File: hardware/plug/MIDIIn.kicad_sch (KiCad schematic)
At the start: 7 parts, among them J401 SJ2-25404B-SMT-TR, U401 74AHC1G125

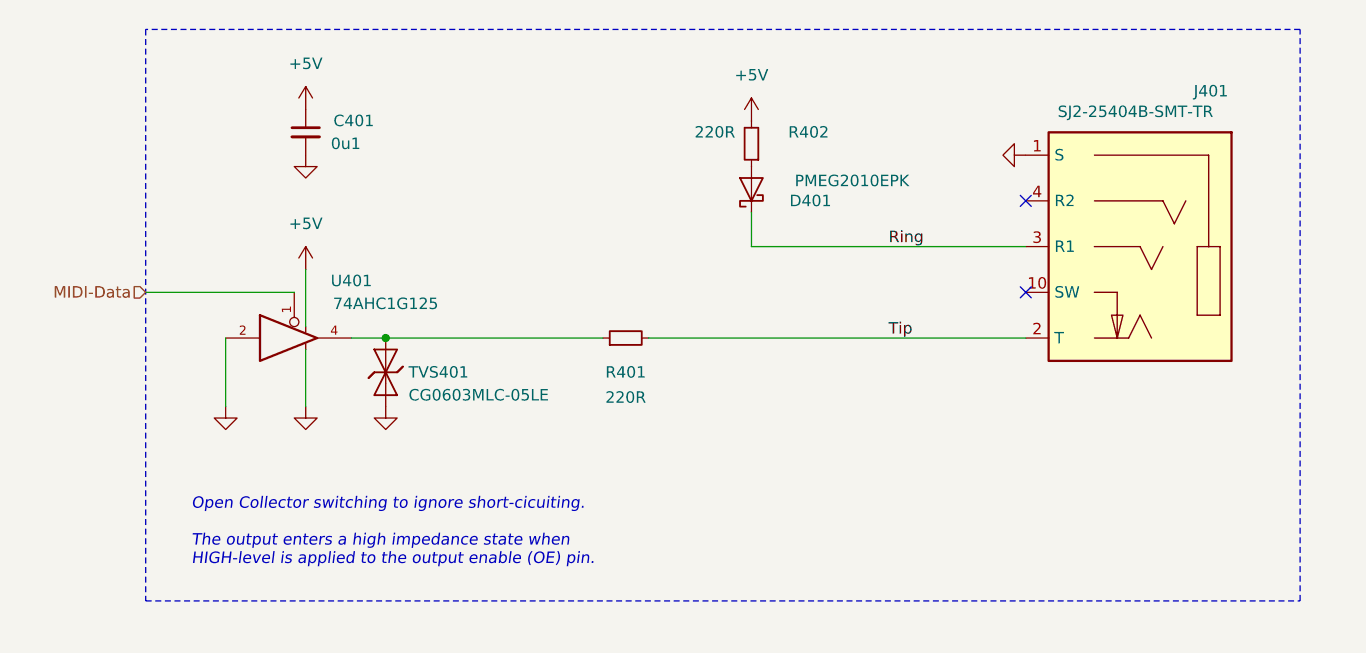
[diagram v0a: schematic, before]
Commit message: Split into socket and plug
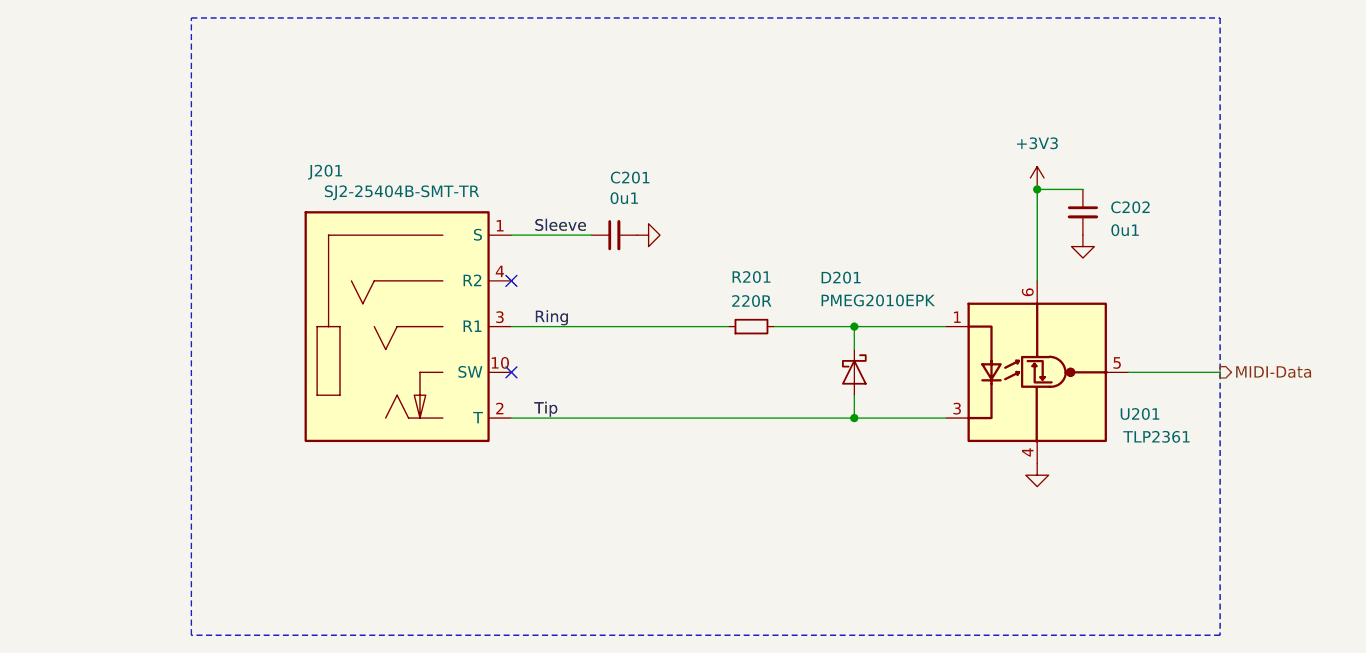
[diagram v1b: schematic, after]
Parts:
- removed C401: 0u1, V2_Capacitor_SMD:C_0603, symbol V2_Capacitor:0603_0u1
- removed D401: PMEG2010EPK, V2_Diode_SMD:D_SOD-1608, symbol V2_Diode:PMEG2010EPK
- removed J401: SJ2-25404B-SMT-TR, V2_Connector_Audio:CUI_SJ2-25404B-SMT-TR, symbol V2_Connector_Audio:SJ2-25404B-SMT-TR
- removed R401, R402: 220R, V2_Resistor_SMD:R_0603, symbol V2_Resistor:0603_220R
- removed TVS401: CG0603MLC-05LE, V2_Diode_SMD:D_0603, symbol V2_Diode:CG0603MLC-05LE
- removed U401: 74AHC1G125, V2_Package_TO_SOT_SMD:SOT-23-5, symbol V2_74xGxx:74AHC1G125
- added C201, C202: 0u1, V2_Capacitor_SMD:C_0603, symbol V2_Capacitor:0603_0u1
- added D201: PMEG2010EPK, V2_Diode_SMD:D_SOD-1608, symbol V2_Diode:PMEG2010EPK
- added J201: SJ2-25404B-SMT-TR, V2_Connector_Audio:CUI_SJ2-25404B-SMT-TR, symbol V2_Connector_Audio:SJ2-25404B-SMT-TR
- added R201: 220R, V2_Resistor_SMD:R_0603, symbol V2_Resistor:0603_220R
- added U201: TLP2361, V2_Package_SO:SO-5-6_4.55x3.7mm_P1.27mm, symbol V2_Isolator:TLP2361
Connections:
- net GND: now also C201.2, C202.2, U201.4 (GND)
- net MIDI-Data: now also U201.5 (VO)
- net Ring: now also J201.3 (R1), R201.1
- net Tip: now also D201.2 (A), J201.2 (T), U201.3 (K)
- new net: D201.1 (K), R201.2, U201.1 (A)
- new net +3V3: C202.1, U201.6 (VDD)
- new net Sleeve: C201.1, J201.1 (S)
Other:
- note removed: "﻿Open Collector switching to ignore short-cicuiting. The output enters a high impedance state when HIGH-level is applied to the output enable (OE) pin."
- title: V2 connect -> V2 connect-plug

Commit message: Good Bye Imperial
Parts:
- C201, C202: footprint V2_Capacitor_SMD:C_0603 -> V2_Capacitor_SMD:C_1608; symbol V2_Capacitor:0603_0u1 -> V2_Capacitor:1608_0u1
- R201: footprint V2_Resistor_SMD:R_0603 -> V2_Resistor_SMD:R_1608; symbol V2_Resistor:0603_220R -> V2_Resistor:1608_220R

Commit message: Refresh
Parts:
- renumbered C201 to C401, C202 to C402, D201 to D401, J201 to J401, R201 to R401, U201 to U401
